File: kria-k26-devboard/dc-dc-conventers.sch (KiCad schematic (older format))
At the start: 92 parts, among them U10 AP62301WU-7, U11 AP62301WU-7, U3 AP62301WU-7, U4 AP62301WU-7, U5 AP62301WU-7, U6 AP62301WU-7, U7 AP62301WU-7, U8 RPX-4.0-R, U9 AP62301WU-7

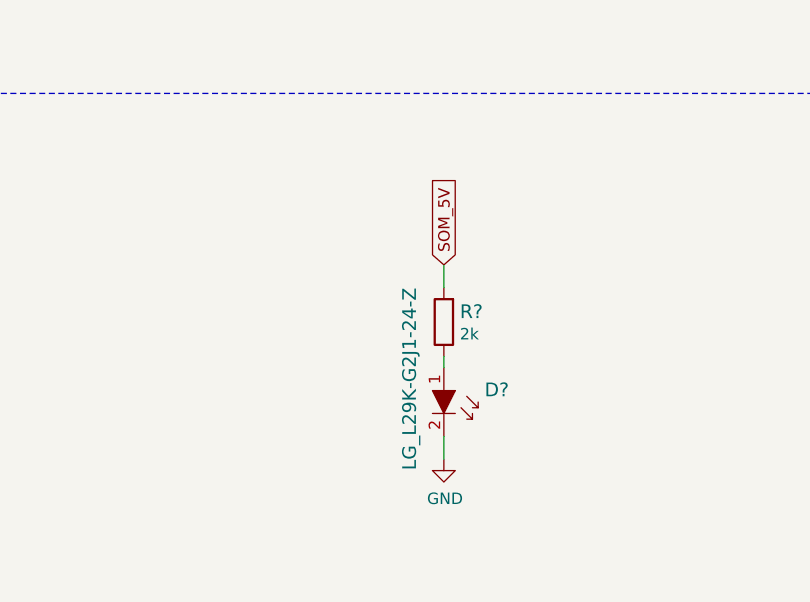
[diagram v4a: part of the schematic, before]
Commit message: Finished tidying up the schematic
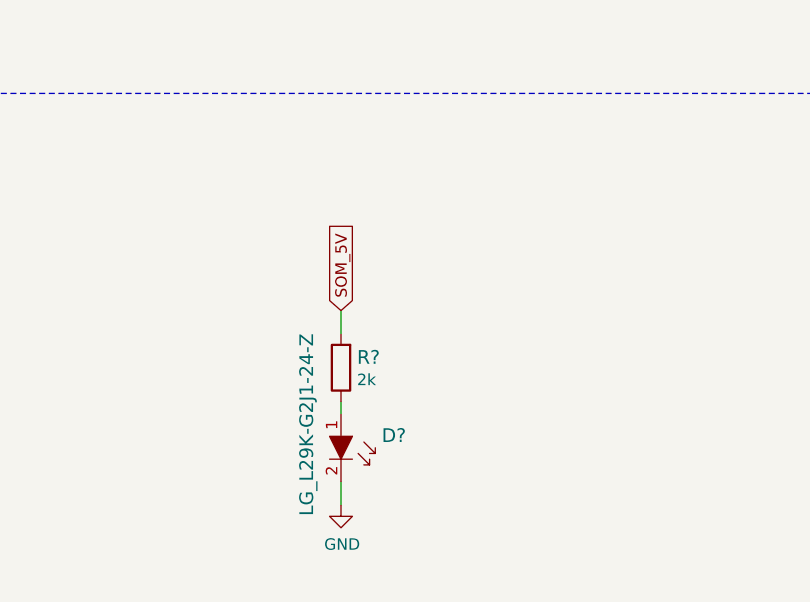
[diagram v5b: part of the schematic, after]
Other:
- moved on the sheet: D?, R?
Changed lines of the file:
@@
 $Descr A3 16535 11693
 encoding utf-8
-Sheet 4 19
+Sheet 16 19
 Title ""
 Date ""
@@
 L antmicroLEDIndicationDiscrete:LG_L29K-G2J1-24-Z D?
 U 1 1 6256D61A
-P 2900 10200
-F 0 "D?" V 2797 10378 60  0000 L CNN
-F 1 "LG_L29K-G2J1-24-Z" H 2350 10050 60  0000 L CNN
-F 2 "antmicro-footprints:LED_0603" H 3100 10400 60  0001 L CNN
-F 3 "https://dammedia.osram.info/media/resource/hires/osram-dam-2493945/LG%20L29K.pdf" H 3100 10500 60  0001 L CNN
-F 4 "LG L29K-G2J1-24-Z" H 3100 10700 60  0001 L CNN "MPN"
-F 5 "OSRAM Opto Semiconductors Inc." H 3100 11300 60  0001 L CNN "Manufacturer"
-	1    2900 10200
+P 2450 10400
+F 0 "D?" V 2347 10578 60  0000 L CNN
+F 1 "LG_L29K-G2J1-24-Z" H 1900 10250 60  0000 L CNN
+F 2 "antmicro-footprints:LED_0603" H 2650 10600 60  0001 L CNN
+F 3 "https://dammedia.osram.info/media/resource/hires/osram-dam-2493945/LG%20L29K.pdf" H 2650 10700 60  0001 L CNN
+F 4 "LG L29K-G2J1-24-Z" H 2650 10900 60  0001 L CNN "MPN"
+F 5 "OSRAM Opto Semiconductors Inc." H 2650 11500 60  0001 L CNN "Manufacturer"
+	1    2450 10400
 	0    1    1    0
 $EndComp
@@
 L antmicroResistors0402:R_2k_0402 R?
 U 1 1 625DCF0C
-P 2900 9800
-F 0 "R?" V 2945 9730 60  0000 R CNN
-F 1 "R_2k_0402" H 2900 9650 60  0001 C CNN
-F 2 "antmicro-footprints:0402-res" H 3100 10000 60  0001 L CNN
-F 3 "" H 2900 9800 50  0001 C CNN
-F 4 "VISHAY" H 3100 10200 60  0001 L CNN "Manufacturer"
-F 5 "CRCW04022K00FKED" H 3100 10100 60  0001 L CNN "MPN"
-F 6 "2k" V 2847 9730 50  0000 R CNN "Val"
-	1    2900 9800
+P 2450 10000
+F 0 "R?" V 2495 9930 60  0000 R CNN
+F 1 "R_2k_0402" H 2450 9850 60  0001 C CNN
+F 2 "antmicro-footprints:0402-res" H 2650 10200 60  0001 L CNN
+F 3 "" H 2450 10000 50  0001 C CNN
+F 4 "VISHAY" H 2650 10400 60  0001 L CNN "Manufacturer"
+F 5 "CRCW04022K00FKED" H 2650 10300 60  0001 L CNN "MPN"
+F 6 "2k" V 2397 9930 50  0000 R CNN "Val"
+	1    2450 10000
 	0    -1   -1   0
 $EndComp
 Wire Wire Line
-	2900 10000 2900 9950
-Text GLabel 2900 9550 1    50   Input ~ 0
+	2450 10200 2450 10150
+Text GLabel 2450 9750 1    50   Input ~ 0
 SOM_5V
 Wire Wire Line
-	2900 9650 2900 9550
+	2450 9850 2450 9750
 $Comp
 L power:GND #PWR?
@@
 L power:GND #PWR?
 U 1 1 62658282
-P 2900 10400
+P 2450 10600
 AR Path="/63C44BC2/62658282" Ref="#PWR?"  Part="1"
 AR Path="/63C44BC2/6235D136/62658282" Ref="#PWR?"  Part="1"
 AR Path="/63C44BC2/623E44F4/62658282" Ref="#PWR?"  Part="1"
 AR Path="/63C44BC2/6244F9D5/62658282" Ref="#PWR?"  Part="1"
-F 0 "#PWR?" H 2900 10150 50  0001 C CNN
-F 1 "GND" H 2905 10227 50  0000 C CNN
-F 2 "" H 2900 10400 50  0001 C CNN
-F 3 "" H 2900 10400 50  0001 C CNN
-	1    2900 10400
-	1    0    0    -1
-$EndComp
-Wire Wire Line
-	2900 10300 2900 10400
+F 0 "#PWR?" H 2450 10350 50  0001 C CNN
+F 1 "GND" H 2455 10427 50  0000 C CNN
+F 2 "" H 2450 10600 50  0001 C CNN
+F 3 "" H 2450 10600 50  0001 C CNN
+	1    2450 10600
+	1    0    0    -1
+$EndComp
+Wire Wire Line
+	2450 10500 2450 10600
 Text GLabel 7850 10250 0    50   Input ~ 0
 PS_1V2

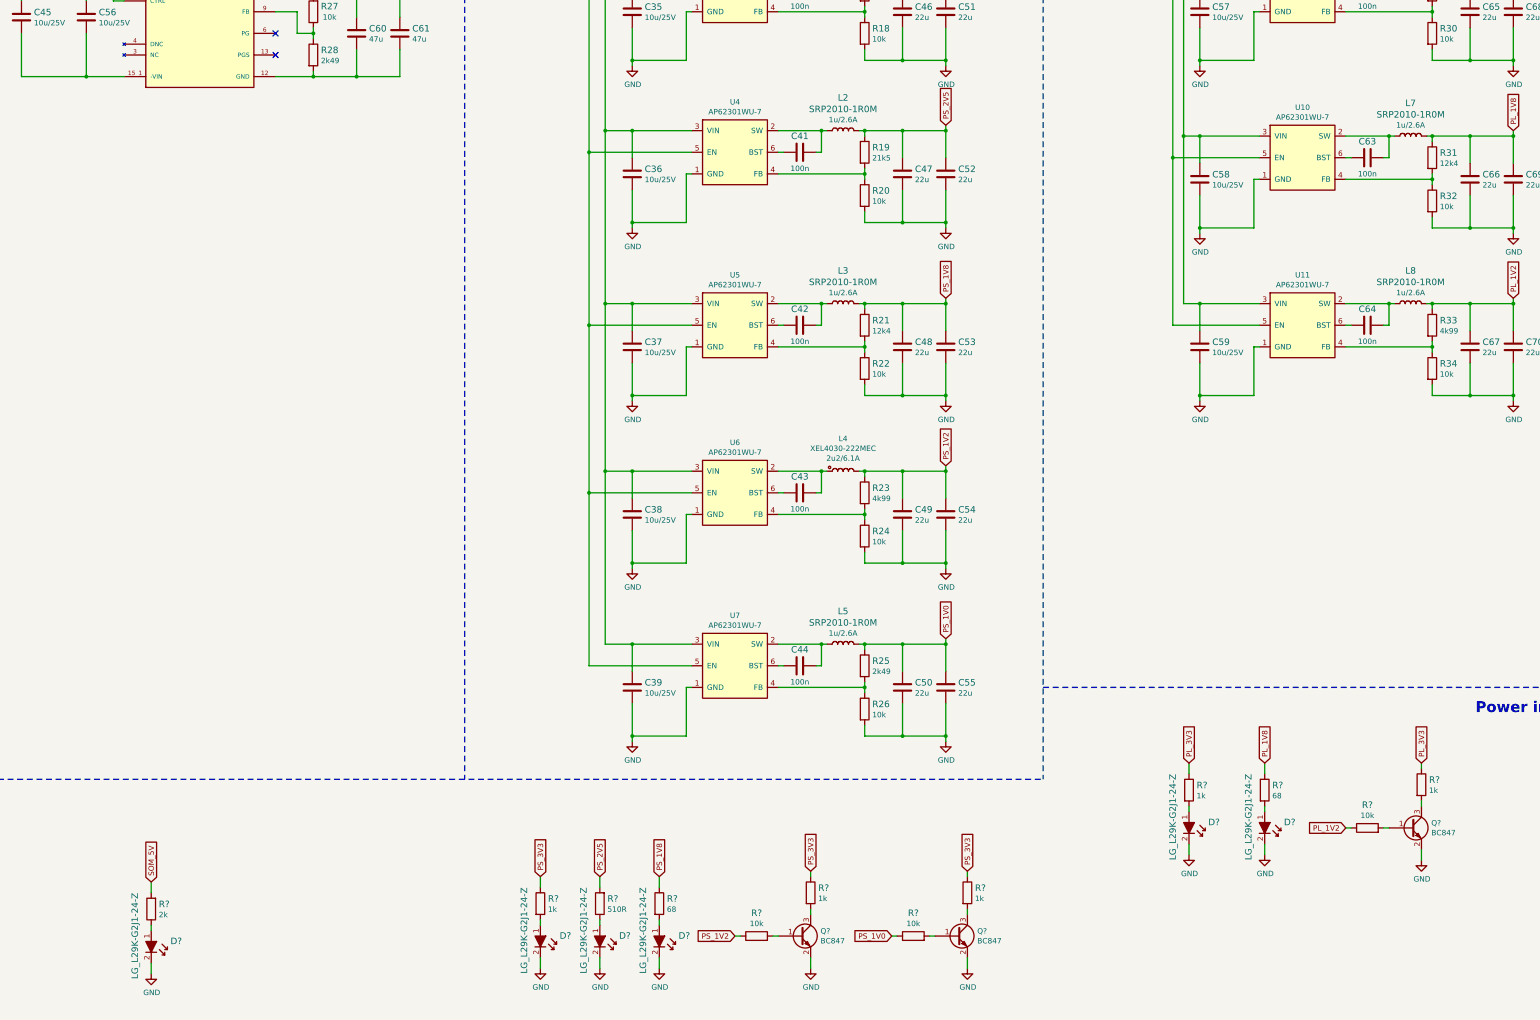
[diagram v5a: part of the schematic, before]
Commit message: Initial placement of power supply
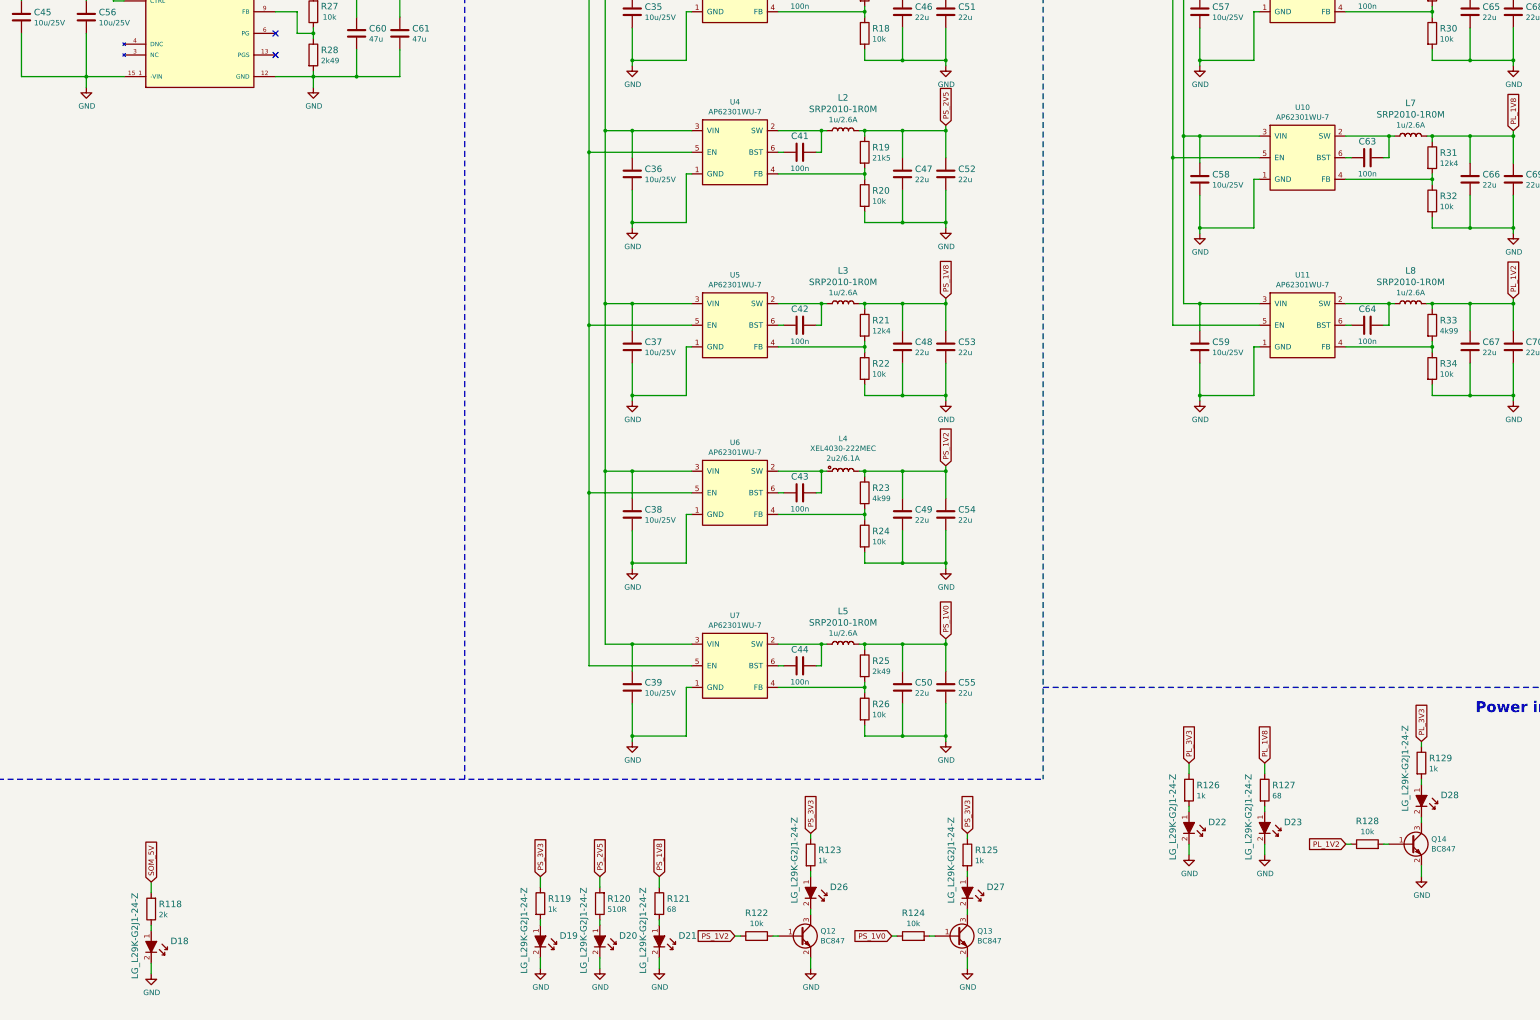
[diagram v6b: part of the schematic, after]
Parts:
- added D26, D27, D28: LG_L29K-G2J1-24-Z, antmicro-footprints:LED_0603, symbol antmicroLEDIndicationDiscrete:LG_L29K-G2J1-24-Z
- gave numbers to parts that had none: 21
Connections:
- net GND: now also C45.2, C56.2, C60.2, C61.2, R28.2, U8.12 (GND), U8.15_1 (-VIN), U8.15_10 (-VIN), U8.15_11 (-VIN), U8.15_12 (-VIN), U8.15_2 (-VIN), U8.15_3 (-VIN), U8.15_4 (-VIN), U8.15_5 (-VIN), U8.15_6 (-VIN), U8.15_7 (-VIN), U8.15_8 (-VIN), U8.15_9 (-VIN)
- net at R123.2: now also D26.1; no longer Q12.3 (C)
- net at R125.2: now also D27.1; no longer Q13.3 (C)
- net at R129.2: now also D28.1; no longer Q14.3 (C)
- new net: D26.2, Q12.3 (C)
- new net: D27.2, Q13.3 (C)
- new net: D28.2, Q14.3 (C)
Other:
- moved on the sheet: Q14, R123, R125, R128, R129

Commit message: Progress in PCB placement
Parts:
- removed Q12, Q13, Q14: BC847, antmicro-footprints:SOT-23-3, symbol antmicroTransistorsBipolarSingle:BC847
- removed R122, R124, R128: R_10k_0402, antmicro-footprints:0402-res, symbol antmicroResistors0402:R_10k_0402
- added Q12, Q13, Q14: DTC014TEBTL, antmicro-footprints:SOT-416, symbol antmicroTransistorsBipolarSingle:DTC014TEBTL
- renumbered C45 to C165, C56 to C166, C60 to C167, C61 to C168, C35 to C169, C36 to C170, C37 to C171, C38 to C172, C39 to C173, C40 to C174, C41 to C175, C42 to C176, C43 to C177, C44 to C178, C46 to C179, C47 to C180, C48 to C181, C49 to C182, C50 to C183, C51 to C184, C52 to C185, C53 to C186, C54 to C187, C55 to C188, C57 to C189, C58 to C190, C59 to C191, C62 to C192, C63 to C193, C64 to C194, C65 to C195, C66 to C196, C67 to C197, C68 to C198, C69 to C199, C70 to C200, D18 to D14, D19 to D15, D20 to D16, D21 to D17, D26 to D18, D27 to D19, D22 to D20, D23 to D21, D28 to D22, R27 to R100, R28 to R101, R119 to R102, R120 to R103, R121 to R104, R123 to R106, R17 to R107, R18 to R108, R19 to R109, R20 to R110, R21 to R111, R22 to R112, R23 to R113, R24 to R114, R25 to R115, R26 to R116, R125 to R118, R126 to R119, R127 to R120, R129 to R122, R29 to R123, R30 to R124, R31 to R125, R32 to R126, R33 to R127, R34 to R128, R118 to R99, U8 to U37, U3 to U38, U4 to U39, U5 to U40, U6 to U41, U7 to U42, U9 to U43, U10 to U44, U11 to U45
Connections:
- net GND: now also Q12.2 (E), Q13.2 (E), Q14.2 (E)
- net PL_1V2: now also Q14.1 (B)
- net PS_1V0: now also Q13.1 (B)
- net PS_1V2: now also Q12.1 (B)
- net SW_PS_1V0: now reaches C178.1, L5.1 (P), U42.2 (SW)
- net at D18.2: now also Q12.3 (C)
- net at D19.2: now also Q13.3 (C)
- net at D22.2: now also Q14.3 (C)
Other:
- moved on the sheet: D18, D19, D22, R106, R118, R122

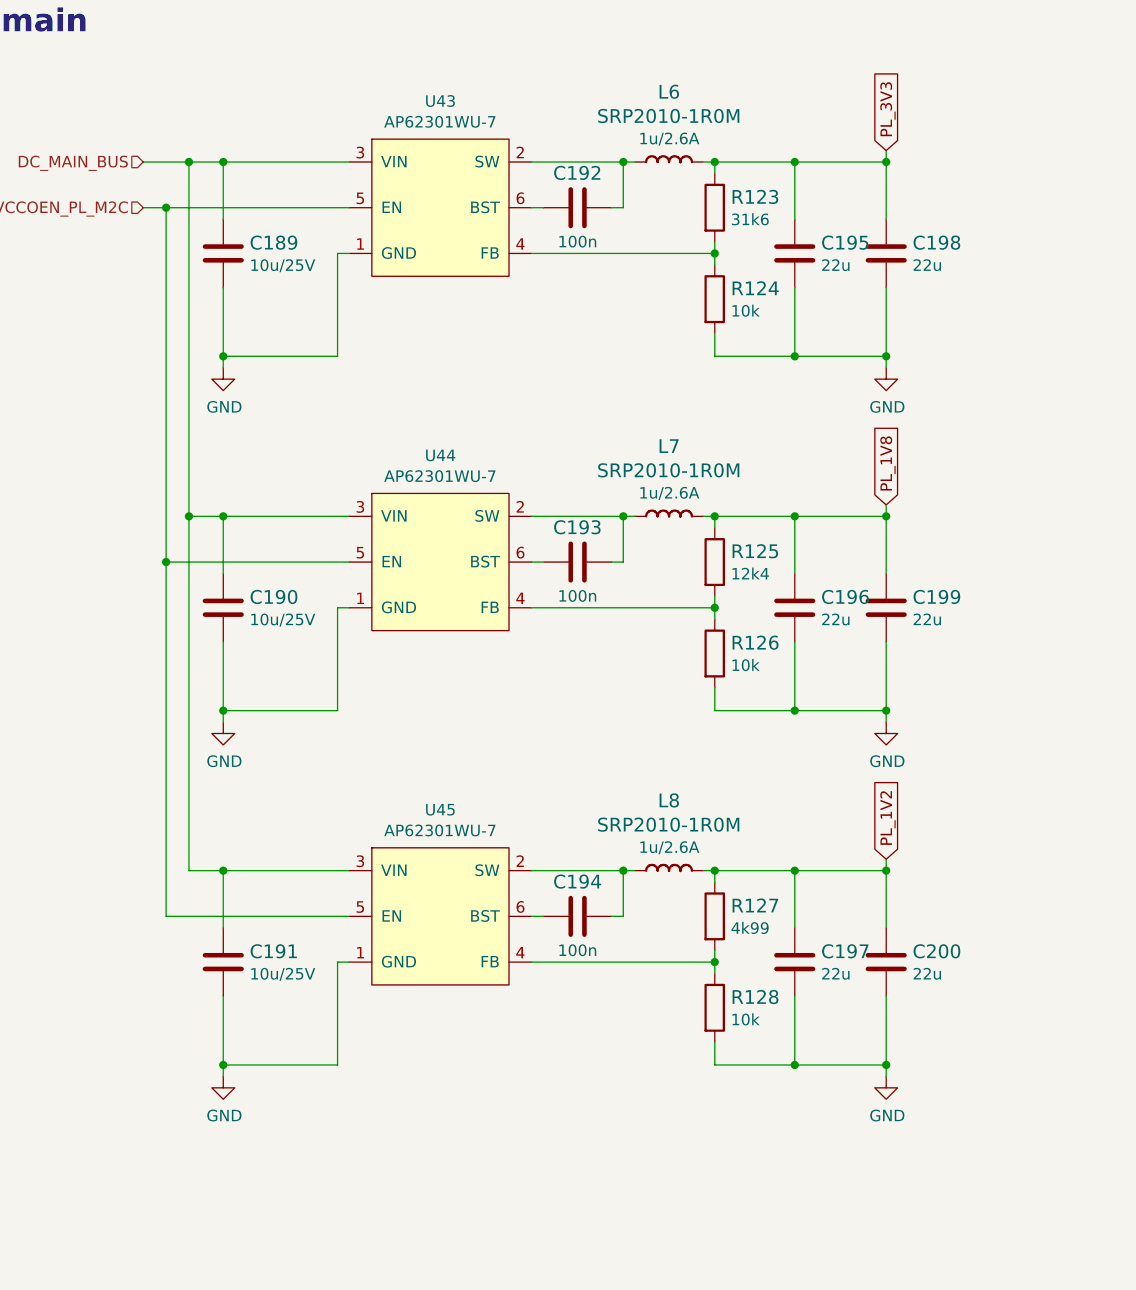
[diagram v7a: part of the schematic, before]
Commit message: Removed PL_1V2 DC-DC, Routed: signalling voltage selector for SD 3.0, reset signals and DC-DC enables, VSYNC, ETH connector diff. pairs, missing USB 3.0 diff. pair. Created planes for PoE adnd DC_MAIN_BUS
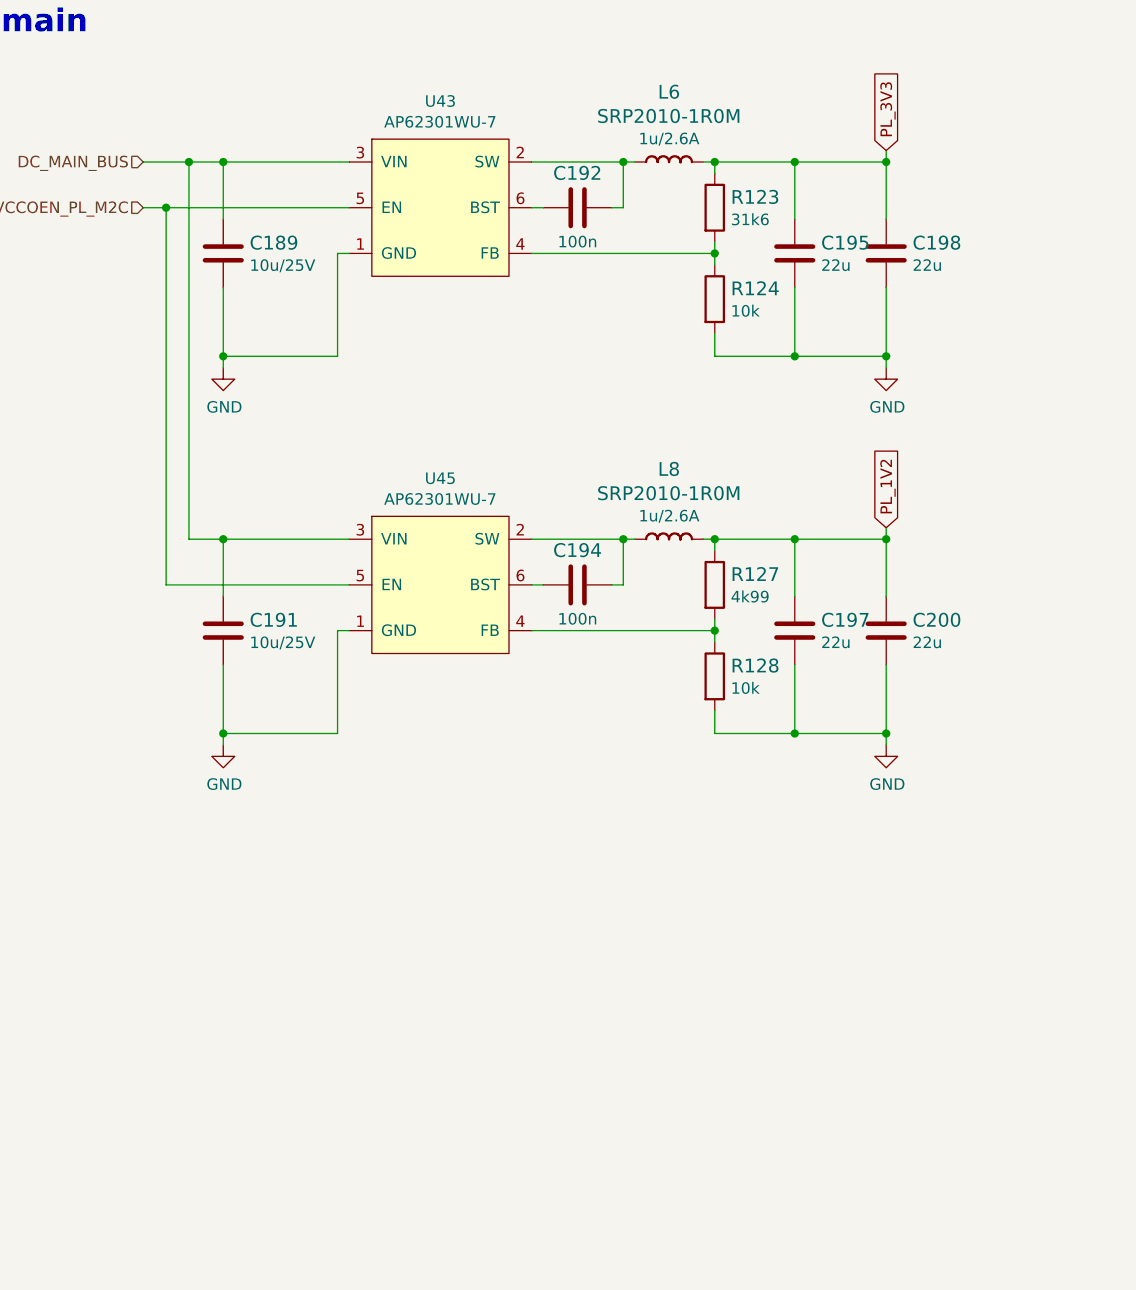
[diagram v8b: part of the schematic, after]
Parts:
- removed C190: C_10u_25V_0603, antmicro-footprints:0603-cap, symbol antmicroCapacitors0603:C_10u_25V_0603
- removed C193: C_100n_0402, antmicro-footprints:0402-cap, symbol antmicroCapacitors0402:C_100n_0402
- removed C196, C199: C_22u_0603, antmicro-footprints:0603-cap, symbol antmicroCapacitors0603:C_22u_0603
- removed L7: SRP2010-1R0M, antmicro-footprints:INDC2016X100N, symbol antmicroFixedInductors:SRP2010-1R0M
- removed R125: R_12k4_0402, antmicro-footprints:0402-res, symbol antmicroResistors0402:R_12k4_0402
- removed R126: R_10k_0402, antmicro-footprints:0402-res, symbol antmicroResistors0402:R_10k_0402
- removed U44: AP62301WU-7, antmicro-footprints:TSOT23-6, symbol antmicroDCDCConverters:AP62301WU-7
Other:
- moved on the sheet: C191, C194, C197, C200, L8, R127, R128, U45
